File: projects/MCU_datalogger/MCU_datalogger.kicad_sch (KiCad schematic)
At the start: 25 parts, among them U1 24LC1025, U2 DS1337S_, U3 24LC1025, U4 ATMEGA328P-AU, Y1 32.768KHz, Y2 16MHz

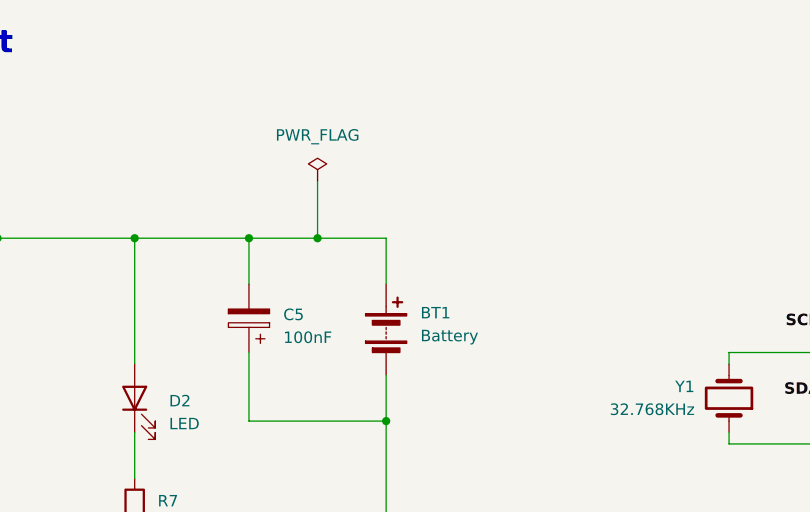
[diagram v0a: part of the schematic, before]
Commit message: MCU datalogger v1.2
- fix missing Vcc label in Battery + net
- fix the resulting violations of Vcc routing (wider tracks required)
- reorder pins of GPIO connector to make Pin 1 is GND
- Add silkscreen labels to connectors I2C ICSP Serial and GPIO
- other minor adjustments to component placements and silkscreen
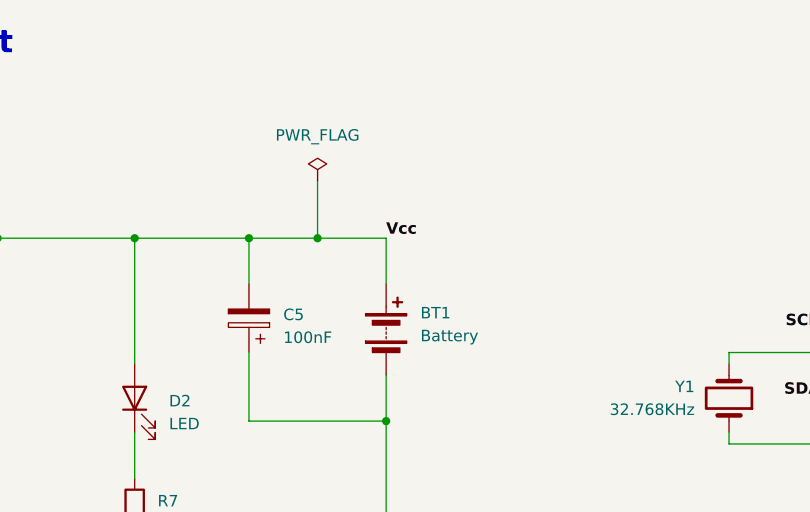
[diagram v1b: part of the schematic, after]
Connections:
- net Vcc: now also BT1.1 (+), C5.2, D2.2 (A), U4.18 (AVCC), U4.4 (VCC)
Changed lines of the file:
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@@
+		)
+	)
+	(label "Vcc"
+		(at 152.4 48.26 0)
+		(effects
+			(font
+				(size 1.27 1.27)
+				(thickness 0.254)
+				(bold yes)
+			)
+			(justify left bottom)
 		)
 	)
